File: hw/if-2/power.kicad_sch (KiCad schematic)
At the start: 15 parts, among them U10 NCP1117-5.0_SOT223, U11 NCP1117-3.3_SOT223

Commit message: First draft of schematic
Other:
- title: (none) -> Power
- moved on the sheet: C41, D1, F1, R28, TP1

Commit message: First draft of schematic
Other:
- note added: "500mA Fuse"
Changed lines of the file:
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@@
+		)
+	)
+	(text "500mA Fuse"
+		(exclude_from_sim no)
+		(at 112.522 104.14 0)
+		(effects
+			(font
+				(size 1.27 1.27)
+			)
 		)
 	)

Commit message: Adding changes suggested by Dan
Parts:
- added CR1: ESDA14V2LY, SOT23-3L_STM, symbol symbol-library-1:ESDA14V2LY
- added D3, D4: D_Schottky, symbol Device:D_Schottky
- C41: value 100u -> 470u
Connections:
- net +12V: now also CR1.1, D3.1 (K), D4.1 (K); no longer F1.2
- net GND: now also CR1.3, D3.2 (A)
- new net: D4.2 (A), F1.2
- no-connect marks 0 -> 1
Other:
- note added: "Board-level filter"
- note added: "TVS Diode (12V_{wm}) for protection against ESD and other over-voltage transients."
- moved on the sheet: C41, D1, R28, TP1

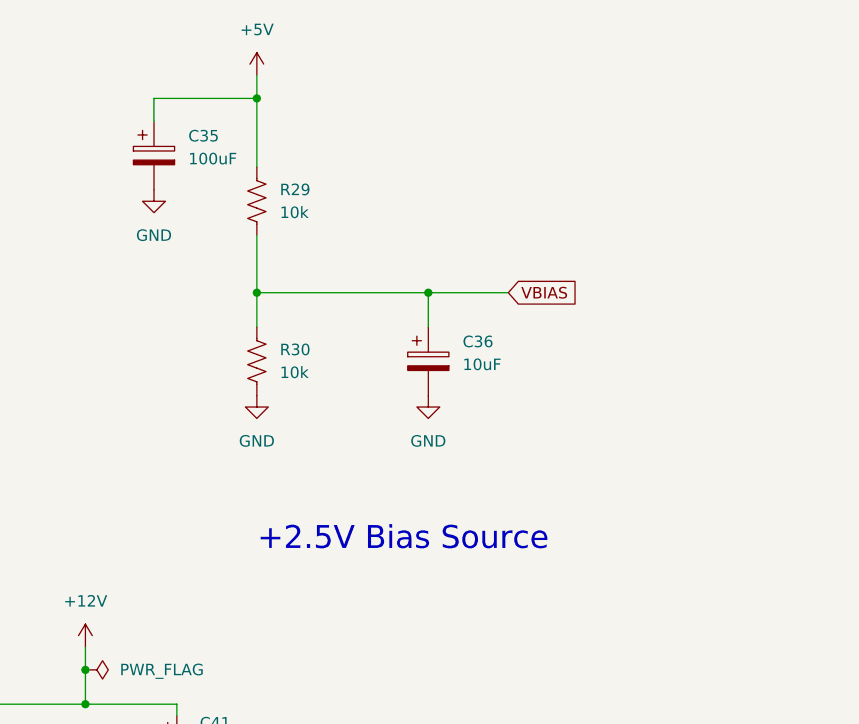
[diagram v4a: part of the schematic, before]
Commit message: Ready to do layout on IF2 board
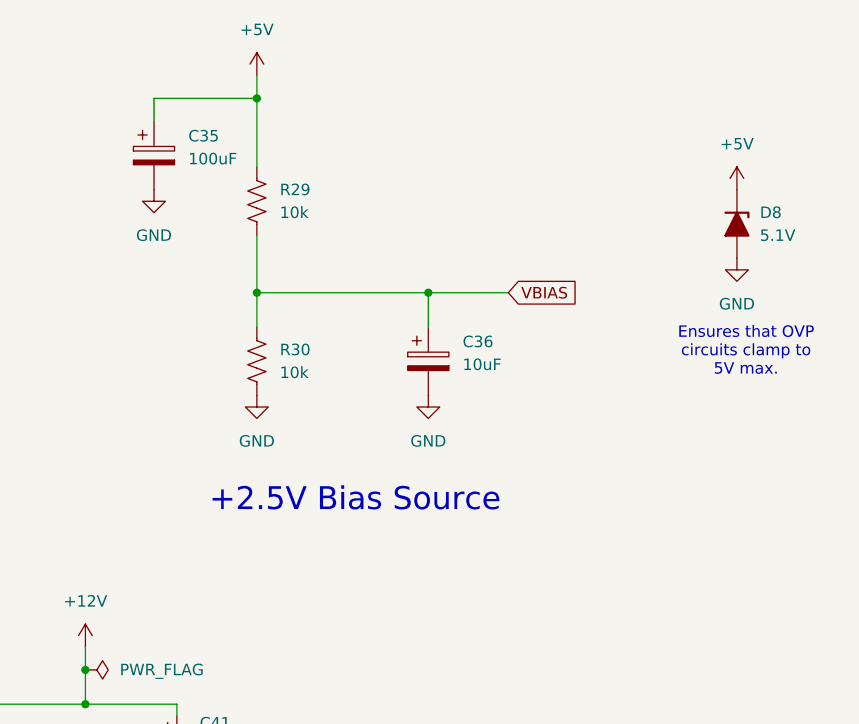
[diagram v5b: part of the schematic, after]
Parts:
- added D8: 5.1V, symbol Device:D_Zener_Filled
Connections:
- net +5V: now also D8.1 (K)
- net GND: now also D8.2 (A)
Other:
- note added: "Ensures that OVP circuits clamp to 5V max."
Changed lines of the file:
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@@
 		)
 	)
+	(text "Ensures that OVP \ncircuits clamp to \n5V max."
+		(exclude_from_sim no)
+		(at 248.666 56.134 0)
+		(effects
+			(font
+				(size 1.27 1.27)
+			)
+		)
+	)
 	(text "Power LED"
 		(exclude_from_sim no)
@@
 	(text "+2.5V Bias Source"
 		(exclude_from_sim no)
-		(at 210.566 76.962 0)
+		(at 205.232 72.644 0)
 		(effects
 			(font
@@
 	)
 	(symbol
+		(lib_id "power:GND")
+		(at 247.65 45.72 0)
+		(unit 1)
+		(exclude_from_sim no)
+		(in_bom yes)
+		(on_board yes)
+		(dnp no)
+		(fields_autoplaced yes)
+		(property "Reference" "#PWR0106"
+			(at 247.65 52.07 0)
+			(effects
+				(font
+					(size 1.27 1.27)
+				)
+				(hide yes)
+			)
+		)
+		(property "Value" "GND"
+			(at 247.65 50.8 0)
+			(effects
+				(font
+					(size 1.27 1.27)
+				)
+			)
+		)
+		(property "Footprint" ""
+			(at 247.65 45.72 0)
+			(effects
+				(font
+					(size 1.27 1.27)
+				)
+				(hide yes)
+			)
+		)
+		(property "Datasheet" ""
+			(at 247.65 45.72 0)
+			(effects
+				(font
+					(size 1.27 1.27)
+				)
+				(hide yes)
+			)
+		)
+		(property "Description" "Power symbol creates a global label with name \"GND\" , ground"
+			(at 247.65 45.72 0)
+			(effects
+				(font
+					(size 1.27 1.27)
+				)
+				(hide yes)
+			)
+		)
+		(pin "1"
+		)
+		(instances
+			(project "if-2"
+				(path "/a8c2d6aa-29bb-49bd-a367-0d62a0a32480/d1654b22-6004-4416-89b1-96259d57a19f"
+					(reference "#PWR0106")
+					(unit 1)
+				)
+			)
+		)
+	)
+	(symbol
 		(lib_id "Device:C_Polarized_Small_US")
 		(at 139.7 45.72 0)
@@
 	)
 	(symbol
+		(lib_id "Device:D_Zener_Filled")
+		(at 247.65 41.91 270)
+		(unit 1)
+		(exclude_from_sim no)
+		(in_bom yes)
+		(on_board yes)
+		(dnp no)
+		(fields_autoplaced yes)
+		(property "Reference" "D8"
+			(at 250.19 40.6399 90)
+			(effects
+				(font
+					(size 1.27 1.27)
+				)
+				(justify left)
+			)
+		)
+		(property "Value" "5.1V"
+			(at 250.19 43.1799 90)
+			(effects
+				(font
+					(size 1.27 1.27)
+				)
+				(justify left)
+			)
+		)
+		(property "Footprint" ""
+			(at 247.65 41.91 0)
+			(effects
+				(font
+					(size 1.27 1.27)
+				)
+				(hide yes)
+			)
+		)
+		(property "Datasheet" "~"
+			(at 247.65 41.91 0)
+			(effects
+				(font
+					(size 1.27 1.27)
+				)
+				(hide yes)
+			)
+		)
+		(property "Description" "Zener diode, filled shape"
+			(at 247.65 41.91 0)
+			(effects
+				(font
+					(size 1.27 1.27)
+				)
+				(hide yes)
+			)
+		)
+		(pin "1"
+		)
+		(pin "2"
+		)
+		(instances
+			(project "if-2"
+				(path "/a8c2d6aa-29bb-49bd-a367-0d62a0a32480/d1654b22-6004-4416-89b1-96259d57a19f"
+					(reference "D8")
+					(unit 1)
+				)
+			)
+		)
+	)
+	(symbol
 		(lib_id "power:GND")
 		(at 41.91 52.07 0)
@@
 					(unit 1)
 				)
+			)
+		)
+	)
+	(symbol
+		(lib_id "power:+5V")
+		(at 247.65 38.1 0)
+		(unit 1)
+		(exclude_from_sim no)
+		(in_bom yes)
+		(on_board yes)
+		(dnp no)
+		(fields_autoplaced yes)
+		(property "Reference" "#PWR0105"
+			(at 247.65 41.91 0)
+			(effects
+				(font
+					(size 1.27 1.27)
+				)
+				(hide yes)
+			)
+		)
+		(property "Value" "+5V"
+			(at 247.65 33.02 0)
+			(effects
+				(font
+					(size 1.27 1.27)
+				)
+			)
+		)
+		(property "Footprint" ""
+			(at 247.65 38.1 0)
+			(effects
+				(font
+					(size 1.27 1.27)
+				)
+				(hide yes)
+			)
+		)
+		(property "Datasheet" ""
+			(at 247.65 38.1 0)
+			(effects
+				(font
+					(size 1.27 1.27)
+				)
+				(hide yes)
+			)
+		)
+		(property "Description" "Power symbol creates a global label with name \"+5V\""
+			(at 247.65 38.1 0)
+			(effects
+				(font
+					(size 1.27 1.27)
+				)
+				(hide yes)
+			)
+		)
+		(pin "1"
+		)
+		(instances
+			(project "if-2"
+				(path "/a8c2d6aa-29bb-49bd-a367-0d62a0a32480/d1654b22-6004-4416-89b1-96259d57a19f"
+					(reference "#PWR0105")
+					(unit 1)
+				)

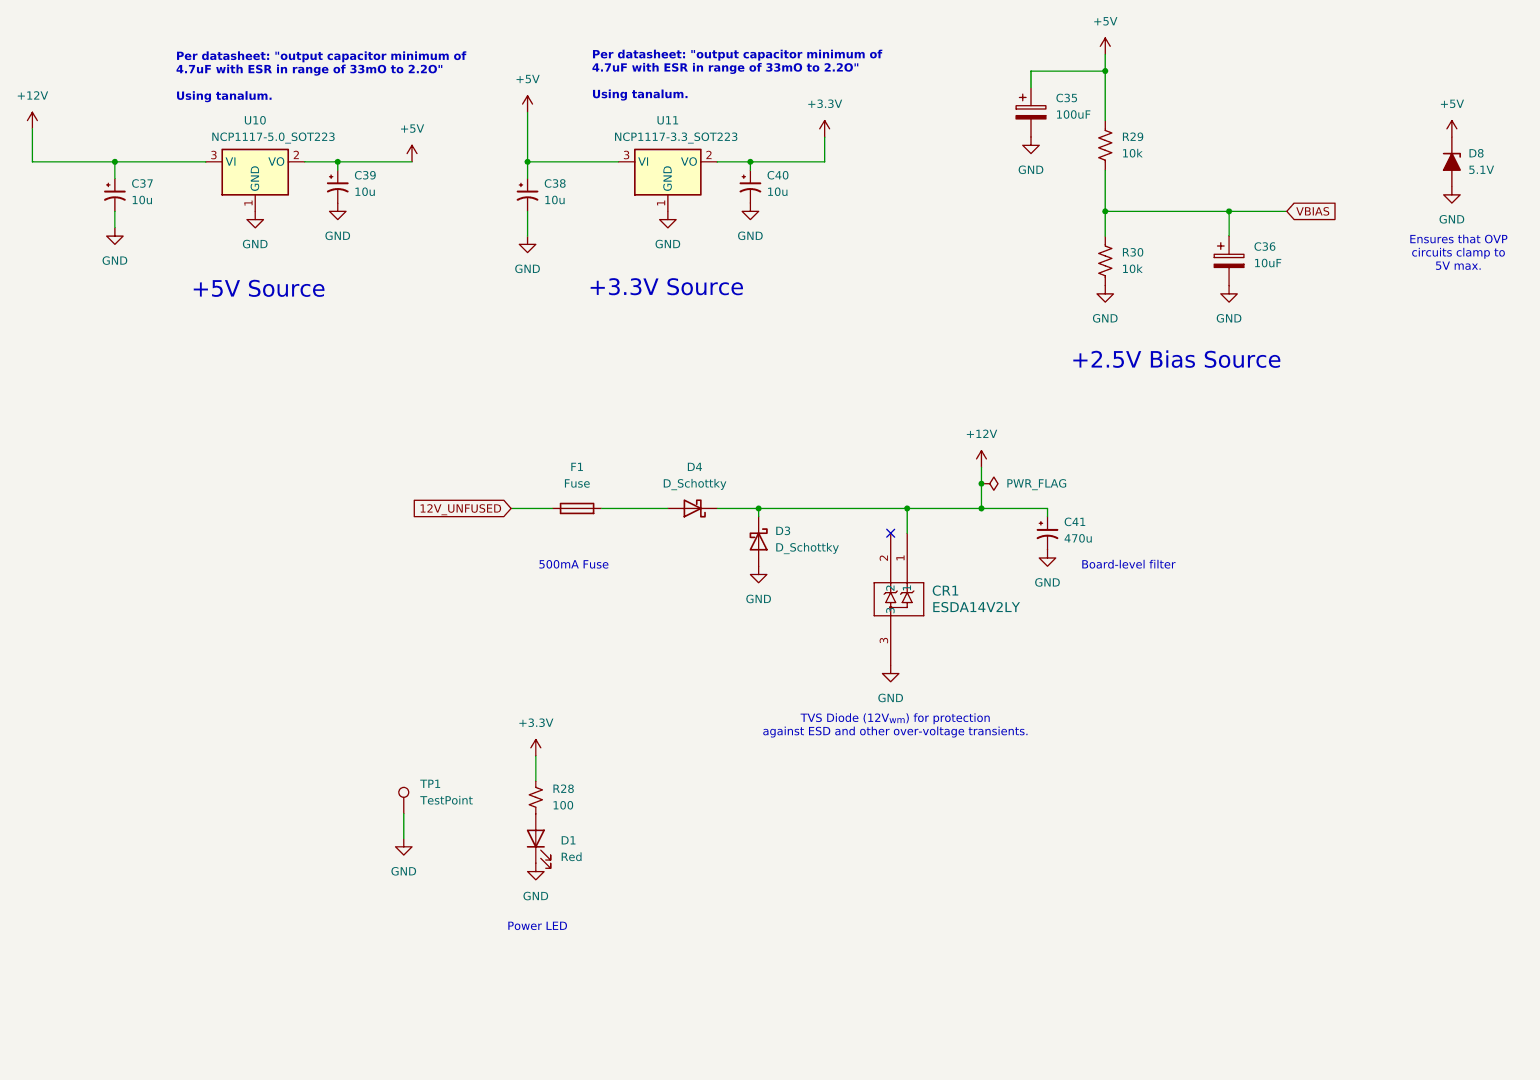
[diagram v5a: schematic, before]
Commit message: Ready to do layout on IF2 board
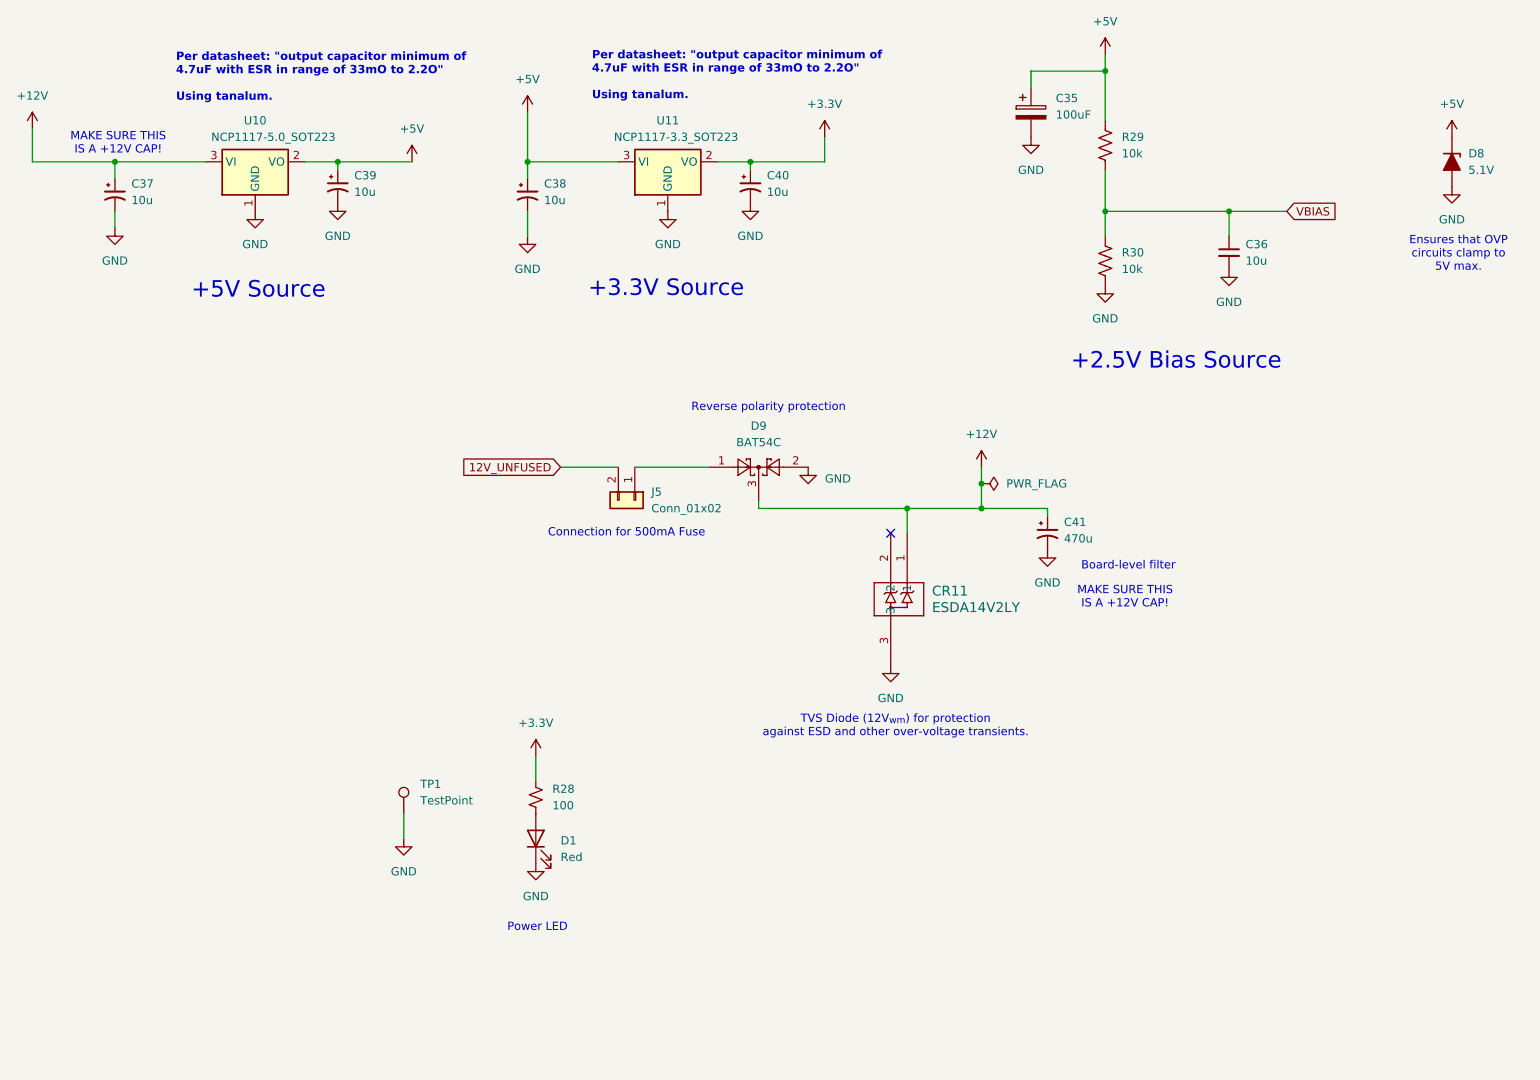
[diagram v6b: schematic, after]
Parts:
- removed C36: 10uF, Capacitor_THT:CP_Radial_D5.0mm_P2.50mm, symbol Device:C_Polarized
- removed CR1: ESDA14V2LY, SOT23-3L_STM, symbol symbol-library-1:ESDA14V2LY
- removed D3, D4: D_Schottky, symbol Device:D_Schottky
- removed F1: Fuse, symbol Device:Fuse
- added C36: 10u, Capacitor_SMD:C_0805_2012Metric_Pad1.18x1.45mm_HandSolder, symbol Device:C_Small
- added CR11: ESDA14V2LY, bruce-footprints:SOT23-3L_STM, symbol symbol-library-1:ESDA14V2LY
- added D9: BAT54C, Package_TO_SOT_SMD:SOT-23, symbol Diode:BAT54C
- added J5: Conn_01x02, Connector_PinHeader_2.54mm:PinHeader_1x02_P2.54mm_Vertical, symbol Connector_Generic:Conn_01x02
- C41: footprint (none) -> Capacitor_THT:CP_Radial_D5.0mm_P2.50mm
- D8: footprint (none) -> Diode_SMD:D_SOD-123
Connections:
- net +12V: now also CR11.1, D9.3
- net 12V_UNFUSED: now also J5.2 (Pin_2)
- net GND: now also C36.2, CR11.3, D9.2
- net VBIAS: now also C36.1
- new net: D9.1, J5.1 (Pin_1)
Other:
- note added: "Connection for 500mA Fuse"
- note added: "MAKE SURE THIS IS A +12V CAP!"
- note added: "Reverse polarity protection"
- note removed: "500mA Fuse"
- title: Power -> COS/CTCSS/PTT Controls (Radio 1)

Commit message: Making progress on layout
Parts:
- added TP10, TP8, TP9: TestPoint, TestPoint:TestPoint_Pad_2.5x2.5mm, symbol Connector:TestPoint
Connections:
- net +3.3V: now also TP9.1
- net +5V: now also TP8.1
- net VBIAS: now also TP10.1
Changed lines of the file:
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@@
+	)
+	(junction
+		(at 87.63 41.91)
+		(diameter 0)
+		(color 0 0 0 0)
+	)
+	(junction
+		(at 151.13 41.91)
+		(diameter 0)
+		(color 0 0 0 0)
 	)
 	(junction
@@
 	)
 	(junction
+		(at 208.28 49.53)
+		(diameter 0)
+		(color 0 0 0 0)
+	)
+	(junction
 		(at 194.31 27.94)
 		(diameter 0)
@@
 	(wire
 		(pts
+			(xy 208.28 49.53) (xy 213.36 49.53)
+		)
+		(stroke
+			(width 0)
+			(type default)
+		)
+	)
+	(wire
+		(pts
 			(xy 105.41 44.45) (xy 105.41 41.91)
 		)
@@
 	(wire
 		(pts
+			(xy 151.13 41.91) (xy 157.48 41.91)
+		)
+		(stroke
+			(width 0)
+			(type default)
+		)
+	)
+	(wire
+		(pts
 			(xy 140.97 95.25) (xy 163.83 95.25)
 		)
@@
 	(wire
 		(pts
+			(xy 87.63 41.91) (xy 91.44 41.91)
+		)
+		(stroke
+			(width 0)
+			(type default)
+		)
+	)
+	(wire
+		(pts
 			(xy 151.13 38.1) (xy 151.13 41.91)
 		)
@@
 	(wire
 		(pts
-			(xy 194.31 49.53) (xy 213.36 49.53)
+			(xy 194.31 49.53) (xy 208.28 49.53)
 		)
 		(stroke
@@
 	)
 	(symbol
+		(lib_id "Connector:TestPoint")
+		(at 157.48 41.91 0)
+		(unit 1)
+		(exclude_from_sim no)
+		(in_bom yes)
+		(on_board yes)
+		(dnp no)
+		(fields_autoplaced yes)
+		(property "Reference" "TP9"
+			(at 160.02 37.3379 0)
+			(effects
+				(font
+					(size 1.27 1.27)
+				)
+				(justify left)
+			)
+		)
+		(property "Value" "TestPoint"
+			(at 160.02 39.8779 0)
+			(effects
+				(font
+					(size 1.27 1.27)
+				)
+				(justify left)
+			)
+		)
+		(property "Footprint" "TestPoint:TestPoint_Pad_2.5x2.5mm"
+			(at 162.56 41.91 0)
+			(effects
+				(font
+					(size 1.27 1.27)
+				)
+				(hide yes)
+			)
+		)
+		(property "Datasheet" "~"
+			(at 162.56 41.91 0)
+			(effects
+				(font
+					(size 1.27 1.27)
+				)
+				(hide yes)
+			)
+		)
+		(property "Description" "test point"
+			(at 157.48 41.91 0)
+			(effects
+				(font
+					(size 1.27 1.27)
+				)
+				(hide yes)
+			)
+		)
+		(pin "1"
+		)
+		(instances
+			(project "if-2"
+				(path "/a8c2d6aa-29bb-49bd-a367-0d62a0a32480/d1654b22-6004-4416-89b1-96259d57a19f"
+					(reference "TP9")
+					(unit 1)
+				)
+			)
+		)
+	)
+	(symbol
 		(lib_id "Device:D_Zener_Filled")
 		(at 247.65 41.91 270)
@@
 	)
 	(symbol
+		(lib_id "Connector:TestPoint")
+		(at 91.44 41.91 0)
+		(unit 1)
+		(exclude_from_sim no)
+		(in_bom yes)
+		(on_board yes)
+		(dnp no)
+		(fields_autoplaced yes)
+		(property "Reference" "TP8"
+			(at 93.98 37.3379 0)
+			(effects
+				(font
+					(size 1.27 1.27)
+				)
+				(justify left)
+			)
+		)
+		(property "Value" "TestPoint"
+			(at 93.98 39.8779 0)
+			(effects
+				(font
+					(size 1.27 1.27)
+				)
+				(justify left)
+			)
+		)
+		(property "Footprint" "TestPoint:TestPoint_Pad_2.5x2.5mm"
+			(at 96.52 41.91 0)
+			(effects
+				(font
+					(size 1.27 1.27)
+				)
+				(hide yes)
+			)
+		)
+		(property "Datasheet" "~"
+			(at 96.52 41.91 0)
+			(effects
+				(font
+					(size 1.27 1.27)
+				)
+				(hide yes)
+			)
+		)
+		(property "Description" "test point"
+			(at 91.44 41.91 0)
+			(effects
+				(font
+					(size 1.27 1.27)
+				)
+				(hide yes)
+			)
+		)
+		(pin "1"
+		)
+		(instances
+			(project "if-2"
+				(path "/a8c2d6aa-29bb-49bd-a367-0d62a0a32480/d1654b22-6004-4416-89b1-96259d57a19f"
+					(reference "TP8")
+					(unit 1)
+				)
+			)
+		)
+	)
+	(symbol
 		(lib_id "power:GND")
 		(at 182.88 38.1 0)
@@
 					(unit 1)
 				)
+			)
+		)
+	)
+	(symbol
+		(lib_id "Connector:TestPoint")
+		(at 208.28 49.53 0)
+		(unit 1)
+		(exclude_from_sim no)
+		(in_bom yes)
+		(on_board yes)
+		(dnp no)
+		(fields_autoplaced yes)
+		(property "Reference" "TP10"
+			(at 210.82 44.9579 0)
+			(effects
+				(font
+					(size 1.27 1.27)
+				)
+				(justify left)
+			)
+		)
+		(property "Value" "TestPoint"
+			(at 210.82 47.4979 0)
+			(effects
+				(font
+					(size 1.27 1.27)
+				)
+				(justify left)
+			)
+		)
+		(property "Footprint" "TestPoint:TestPoint_Pad_2.5x2.5mm"
+			(at 213.36 49.53 0)
+			(effects
+				(font
+					(size 1.27 1.27)
+				)
+				(hide yes)
+			)
+		)
+		(property "Datasheet" "~"
+			(at 213.36 49.53 0)
+			(effects
+				(font
+					(size 1.27 1.27)
+				)
+				(hide yes)
+			)
+		)
+		(property "Description" "test point"
+			(at 208.28 49.53 0)
+			(effects
+				(font
+					(size 1.27 1.27)
+				)
+				(hide yes)
+			)
+		)
+		(pin "1"
+		)
+		(instances
+			(project "if-2"
+				(path "/a8c2d6aa-29bb-49bd-a367-0d62a0a32480/d1654b22-6004-4416-89b1-96259d57a19f"
+					(reference "TP10")
+					(unit 1)
+				)
